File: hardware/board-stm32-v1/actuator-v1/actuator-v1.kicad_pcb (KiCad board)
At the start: 2 copper layers, 82.8 x 64.1 mm, 51 parts, among them IC1 TCAN3413DR, J1 Screw_Terminal_01x02, J2 Screw_Terminal_01x03, J3 Matrix_keyboard, J4 Screw_Terminal_01x13, J5 Conn_01x04_Pin, SW1 SW_Push, U1 TLV75533PDBV, U2 STM32G0B1CBT6, X1 32.768KHz, X2 8MHz

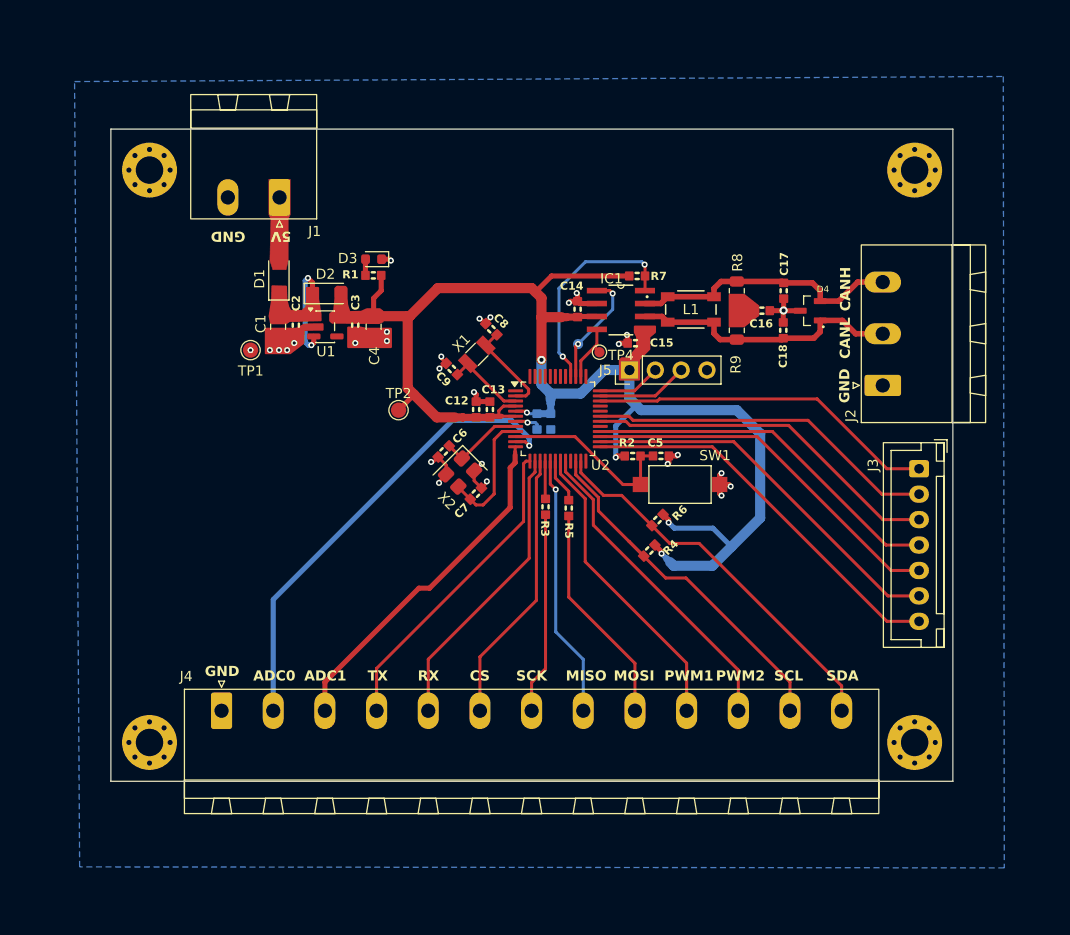
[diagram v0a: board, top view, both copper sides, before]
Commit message: Update actuator PCB layout and schematics
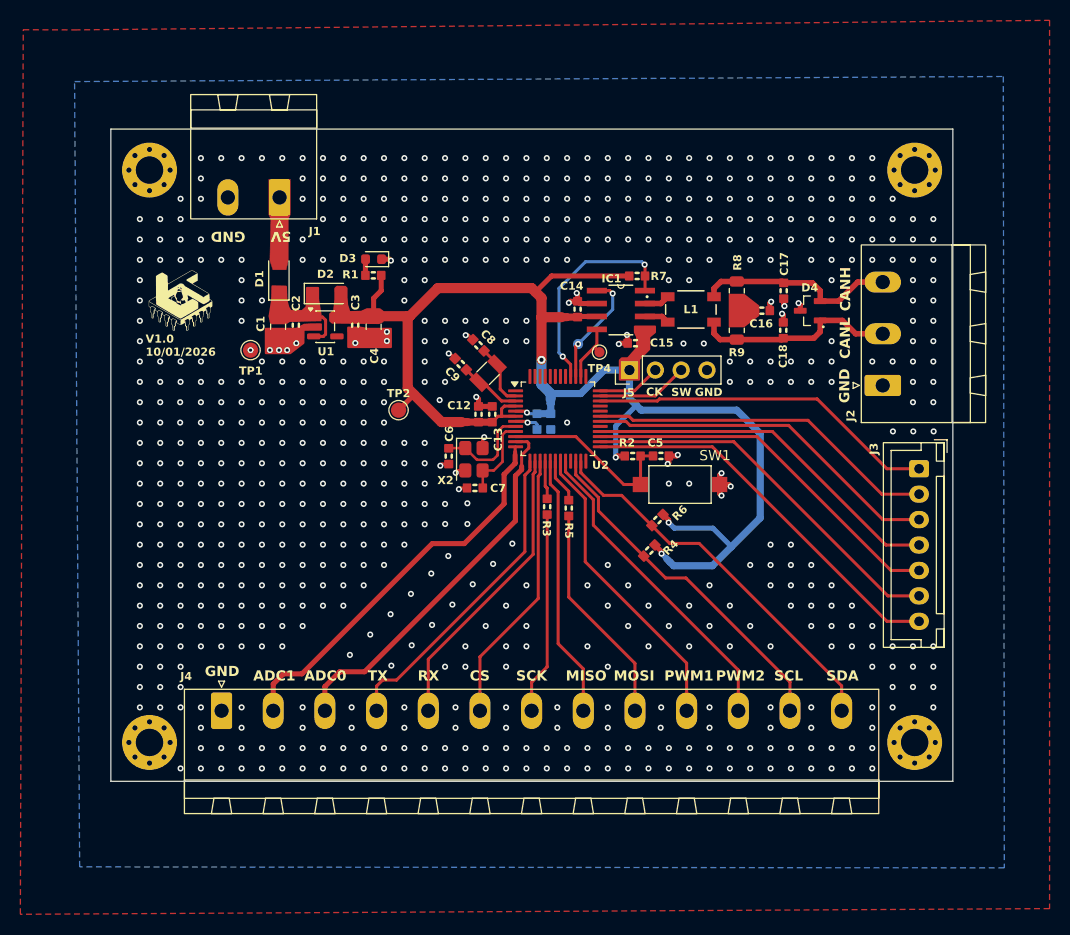
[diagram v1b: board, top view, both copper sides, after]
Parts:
- added G***: LOGO, MY_FOOTPRINTS:logo_trilucas4, F.Cu at (67.9, 50.2)
- moved X1 2.17 mm to (98.3, 57.6)
- moved C8 2.03 mm to (97.4, 54.8)
- moved X2 1.88 mm to (97.0, 66.0), turned to -90 degrees
- moved C9 1.00 mm to (95.7, 56.7)
- moved C6 0.68 mm to (94.5, 65.7), turned to 90 degrees
- moved C7 0.57 mm to (97.1, 68.8), turned to 0 degrees
- moved C13 0.52 mm to (98.8, 61.6)
- moved C12 0.52 mm to (97.4, 61.6)
- moved R3 0.16 mm to (104.2, 70.7)
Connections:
- IC1 pad 6: /TCAN3413/CAN- -> Net-(IC1-CANL)
- IC1 pad 7: /TCAN3413/CAN+ -> Net-(IC1-CANH)
- L1 pad 1: /TCAN3413/CAN+ -> Net-(IC1-CANH)
- L1 pad 2: /TCAN3413/CAN- -> Net-(IC1-CANL)
- U2 pad 11: /MCU-STM32G0B1CBT6/ADC1_IN0 -> /MCU-STM32G0B1CBT6/ADC1_IN1
- U2 pad 12: /MCU-STM32G0B1CBT6/ADC1_IN1 -> /MCU-STM32G0B1CBT6/ADC1_IN0
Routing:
- net /MCU-STM32G0B1CBT6/ADC1_IN0: track 46.4 -> 38.7 mm, vias 1 -> 0
- net GND: track 33.6 -> 26.0 mm, vias 29 -> 665
- net /TCAN3413/CAN+: track 26.9 -> 19.9 mm
- net /TCAN3413/CAN-: track 27.0 -> 19.9 mm
- net /Power5-3V3/+5V: track 9.81 -> 3.92 mm, vias 2 -> 0
- net Net-(U2-PF1): track 12.5 -> 8.12 mm
- net Net-(U2-PC14): track 9.36 -> 6.21 mm
- net /MCU-STM32G0B1CBT6/ADC1_IN1: track 34.3 -> 37.4 mm
- net Net-(IC1-CANH): track 0.00 -> 2.52 mm
- net Net-(IC1-CANL): track 0.00 -> 2.47 mm
- net /MCU-STM32G0B1CBT6/I2C2_SCL: track 36.5 -> 34.4 mm
- net Net-(U2-PC15): track 7.85 -> 6.12 mm
- net Net-(U2-PF0): track 8.34 -> 9.77 mm
- net /MCU-STM32G0B1CBT6/UART_TX: track 31.0 -> 31.6 mm
- net /MCU-STM32G0B1CBT6/SPI_MISO: vias 1 -> 0
- added copper zone on F.Cu, net GND
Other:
- board text added: "CK"
- board text added: "SW"
- board text added: "V1.0 10/01/2026"
